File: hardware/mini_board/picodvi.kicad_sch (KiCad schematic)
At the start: 45 parts, among them J1 USB_A, J5 NOT_HDMI_A, SW1 SW_Push, SW2 SW_Push, U1 RP2040, U2 NCP115ASN330, U3 W25Q16JV, U4 S70KS128, Y1 12 M

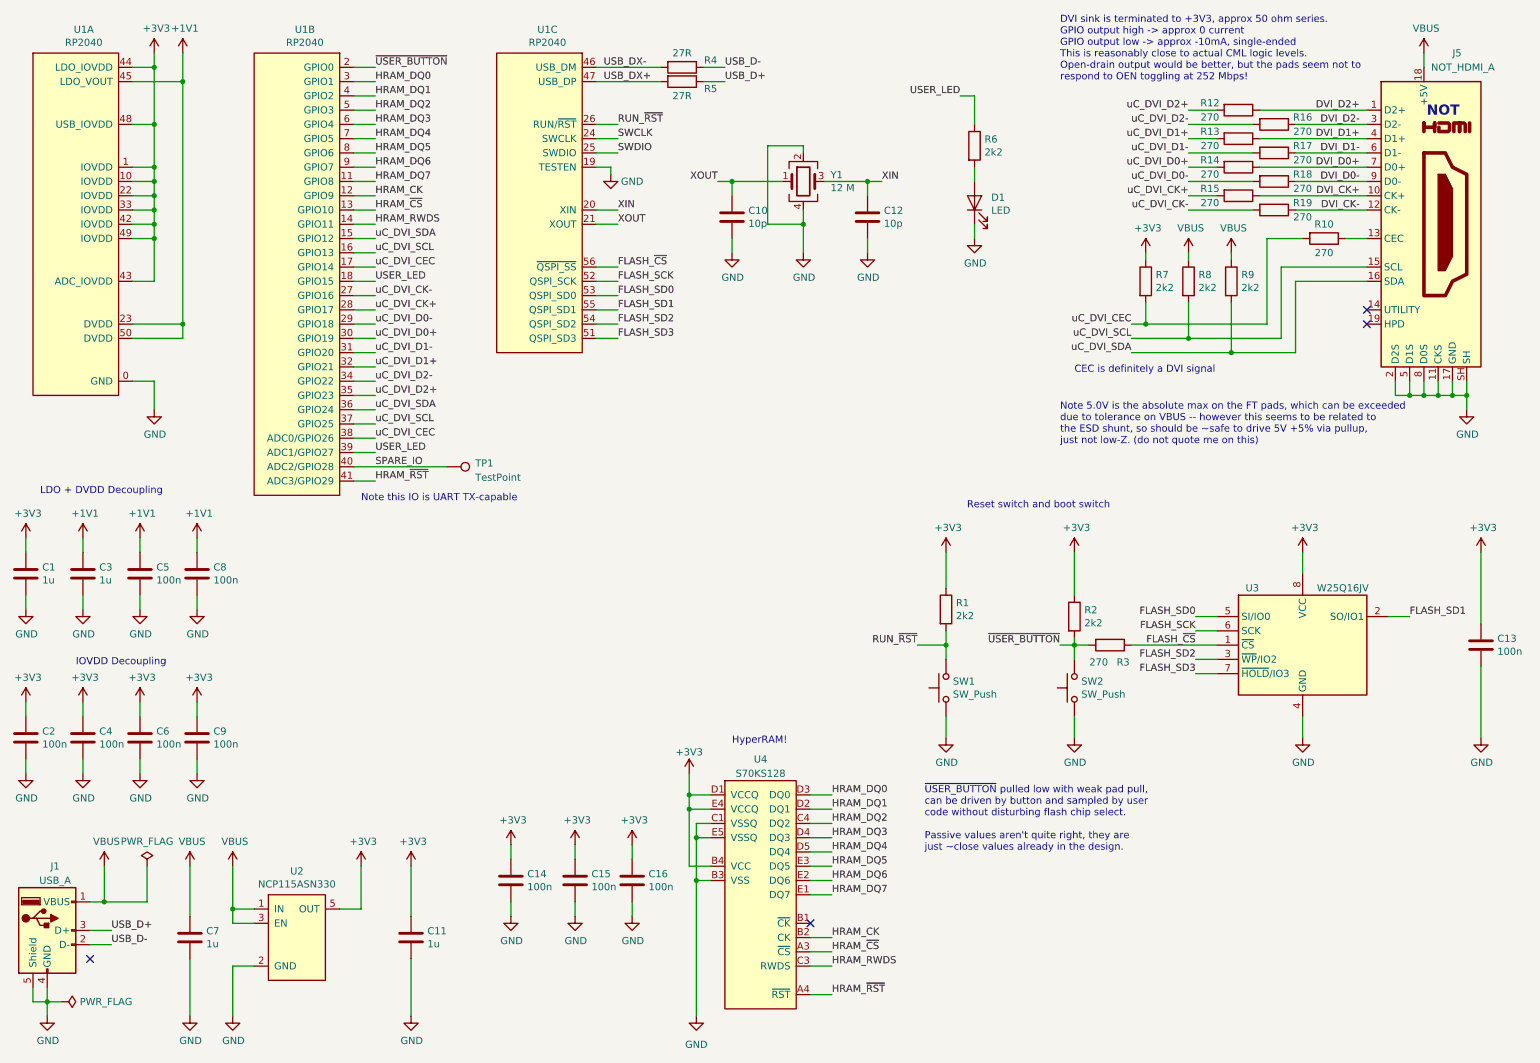
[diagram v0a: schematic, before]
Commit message: Clean up kicad backup stuff in mini board directory
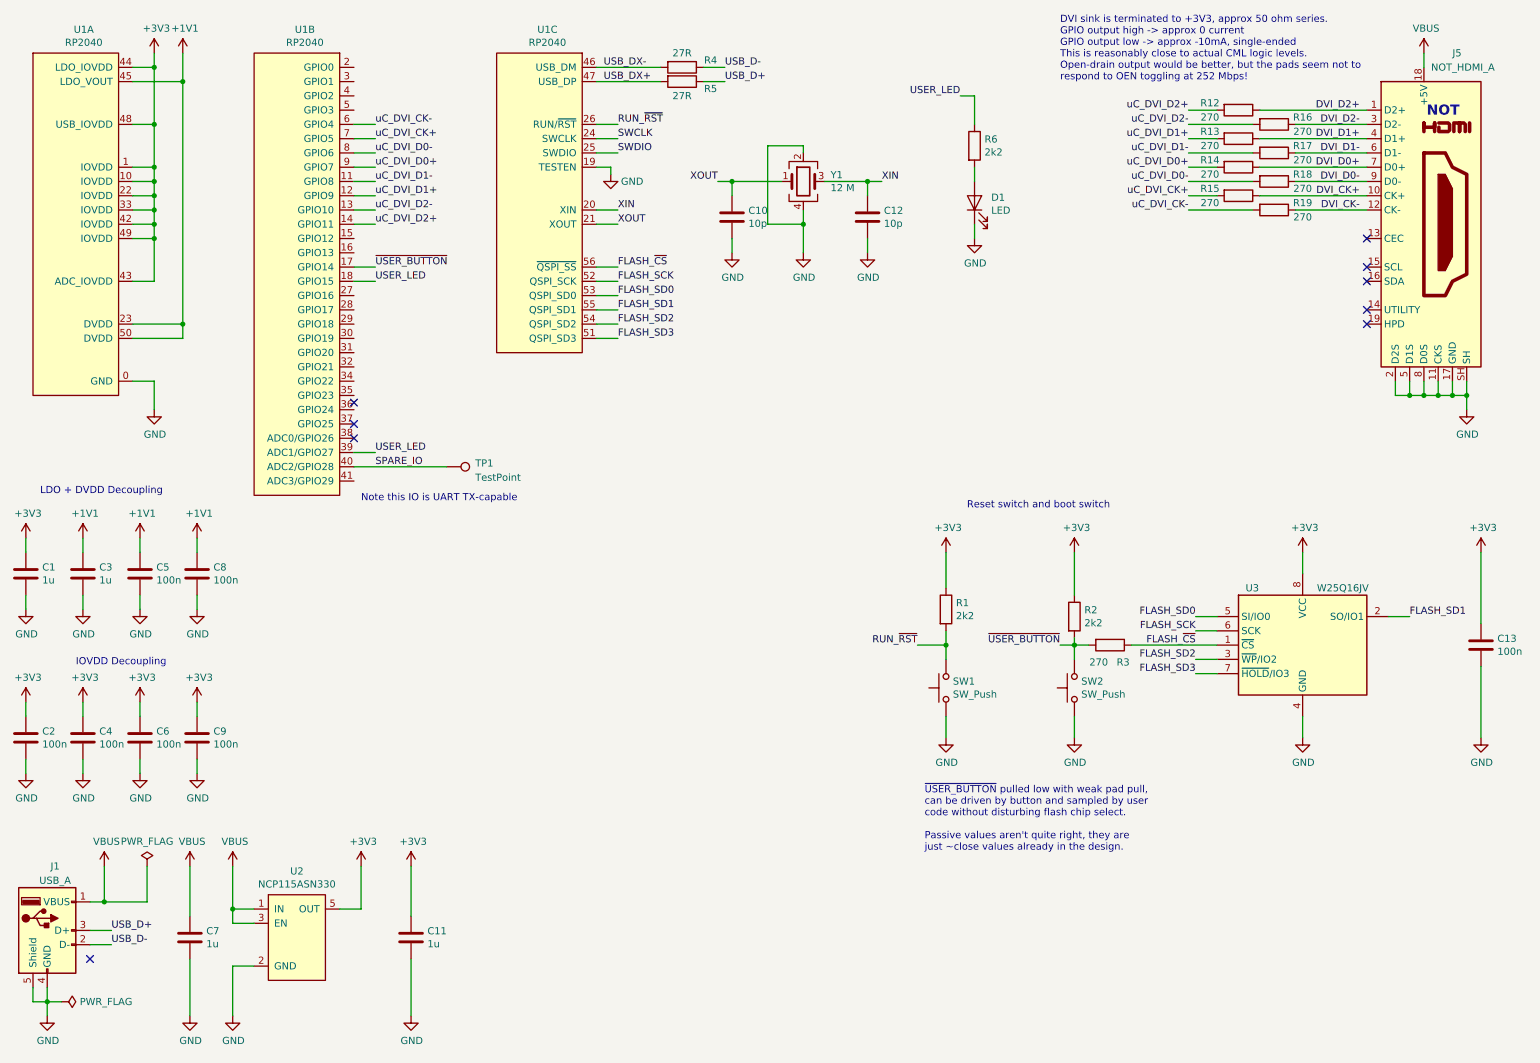
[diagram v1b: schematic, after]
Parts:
- removed C14, C15, C16: 100n, Capacitor_SMD:C_0402_1005Metric, symbol picodvi-rescue:C-Device
- removed R10: 270, Resistor_SMD:R_0402_1005Metric, symbol picodvi-rescue:R-Device
- removed R7, R8, R9: 2k2, Resistor_SMD:R_0402_1005Metric, symbol picodvi-rescue:R-Device
- removed U4: S70KS128, picodvi:S70KS128, symbol picodvi:S70KS128
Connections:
- net HRAM_CK is gone; now on net uC_DVI_D1+: U1.12 (GPIO9)
- net HRAM_DQ3 is gone; now on net uC_DVI_CK-: U1.6 (GPIO4)
- net HRAM_DQ4 is gone; now on net uC_DVI_CK+: U1.7 (GPIO5)
- net HRAM_DQ5 is gone; now on net uC_DVI_D0-: U1.8 (GPIO6)
- net HRAM_DQ6 is gone; now on net uC_DVI_D0+: U1.9 (GPIO7)
- net HRAM_DQ7 is gone; now on net uC_DVI_D1-: U1.11 (GPIO8)
- net HRAM_RWDS is gone; now on net uC_DVI_D2+: U1.14 (GPIO11)
- net HRAM_~CS~ is gone; now on net uC_DVI_D2-: U1.13 (GPIO10)
- net uC_DVI_CK+: no longer U1.28 (GPIO17)
- net uC_DVI_CK-: no longer U1.27 (GPIO16)
- net uC_DVI_D0+: no longer U1.30 (GPIO19)
- net uC_DVI_D0-: no longer U1.29 (GPIO18)
- net uC_DVI_D1+: no longer U1.32 (GPIO21)
- net uC_DVI_D1-: no longer U1.31 (GPIO20)
- net uC_DVI_D2+: no longer U1.35 (GPIO23)
- net uC_DVI_D2-: no longer U1.34 (GPIO22)
- net ~USER_BUTTON~: now also U1.17 (GPIO14); no longer U1.2 (GPIO0)
- net HRAM_DQ0: no longer names the net of U1.3 (GPIO1)
- net HRAM_DQ1: no longer names the net of U1.4 (GPIO2)
- net HRAM_DQ2: no longer names the net of U1.5 (GPIO3)
- net HRAM_~RST~: no longer names the net of U1.41 (ADC3/GPIO29)
- net uC_DVI_CEC: no longer names the net of U1.38 (ADC0/GPIO26)
- net uC_DVI_CEC: no longer U1.17 (GPIO14)
- removed net uC_DVI_SCL: J5.15 (SCL), U1.16 (GPIO13), U1.37 (GPIO25)
- removed net uC_DVI_SDA: J5.16 (SDA), U1.15 (GPIO12), U1.36 (GPIO24)
- no-connect marks 4 -> 9
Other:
- note removed: "CEC is definitely a DVI signal"
- note removed: "HyperRAM!"
- note removed: "Note 5.0V is the absolute max on the FT pads, which can be exceeded due to tolerance on VBUS -- however this seems to be related to the ESD shunt, so should be ~~safe to drive 5V +5% via pullup, just not low-Z. (do not quote me on this)"
